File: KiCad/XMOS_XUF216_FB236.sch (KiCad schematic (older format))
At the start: 20 parts

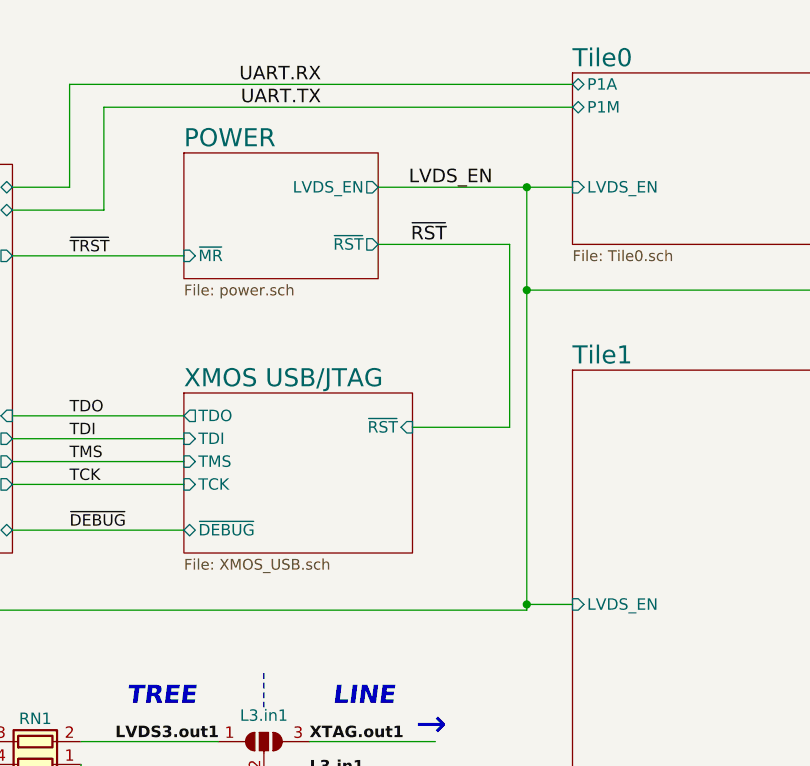
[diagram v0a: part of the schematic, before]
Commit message: Update
Updated to KiCad 5.1.6 and changed the power sheet etc.
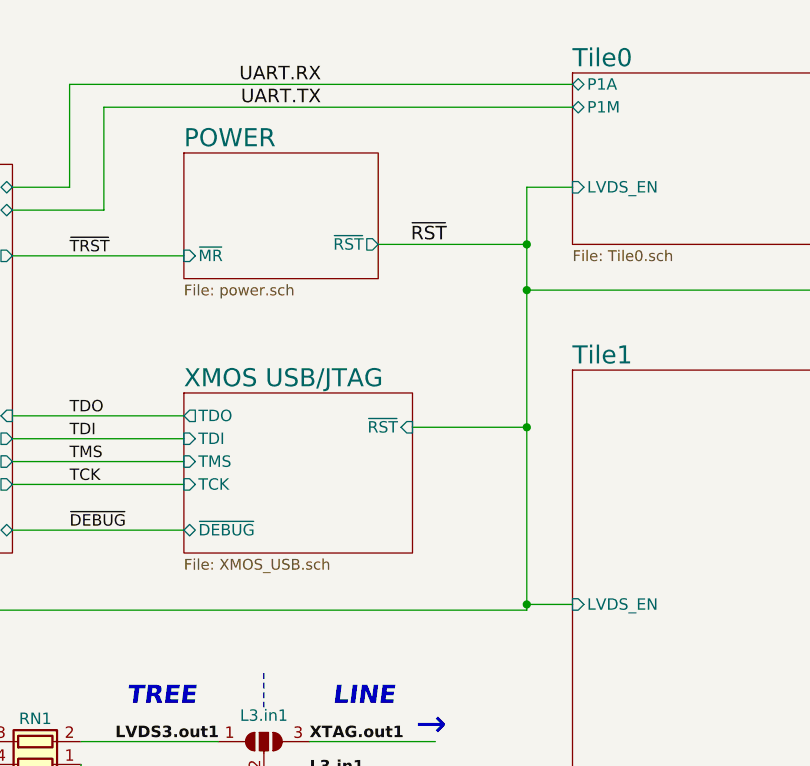
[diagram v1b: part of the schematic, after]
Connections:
- net labels removed: LVDS_EN
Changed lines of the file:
@@
 EESchema Schematic File Version 4
-LIBS:XMOS_XUF216_FB236-cache
-EELAYER 26 0
+EELAYER 30 0
 EELAYER END
 $Descr A4 11693 8268
@@
 Sheet 1 16
 Title "XMOS top level"
-Date "2019-01-08"
-Rev "BETA"
+Date "2020-06-05"
+Rev "BETA 1.1"
 Comp "openPnP"
 Comment1 "Open Source"
@@
 F0 "POWER" 79
 F1 "power.sch" 47
-F2 "LVDS_EN" O R 4250 2175 50
-F3 "~RST" O R 4250 2425 50
-F4 "~MR" I L 3400 2475 50
+F2 "~RST" O R 4250 2425 50
+F3 "~MR" I L 3400 2475 50
 $EndSheet
 $Comp
@@
 	2650 3175 3400 3175
 Wire Wire Line
-	4250 2425 4825 2425
-Wire Wire Line
-	4825 2425 4825 3225
-Wire Wire Line
-	4825 3225 4400 3225
-Wire Wire Line
 	2650 3375 3400 3375
 Wire Wire Line
@@
 Text Label 2900 2475 0    50   ~ 0
 ~TRST
-Text Label 4750 2175 2    59   ~ 0
-LVDS_EN
 Text Label 4550 2425 2    59   ~ 0
 ~RST
-Wire Wire Line
-	4250 2175 4900 2175
 Wire Wire Line
 	2650 2175 2900 2175
@@
 F14 "L4.out1" O R 6650 3425 50
 $EndSheet
-Connection ~ 4900 2175
 Wire Wire Line
 	4900 2175 5100 2175
@@
 Connection ~ 4900 2625
 Wire Wire Line
-	4900 2625 4900 2175
+	4900 2625 4900 2425
 Wire Wire Line
 	11000 4875 11000 3275
@@
 	8400 4000 8400 4125
 Wire Wire Line
-	4900 2625 4900 4000
+	4900 2625 4900 3225
 Wire Wire Line
 	5100 4000 4900 4000
@@
 	1    0    0    -1
 $EndComp
+Connection ~ 4900 2425
+Wire Wire Line
+	4900 2425 4900 2175
+Connection ~ 4900 3225
+Wire Wire Line
+	4900 3225 4900 4000
+Wire Wire Line
+	4250 2425 4900 2425
+Wire Wire Line
+	4400 3225 4900 3225
 $EndSCHEMATC
